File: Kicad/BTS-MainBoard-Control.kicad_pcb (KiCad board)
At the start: 2 copper layers, 26.8 x 45.1 mm, 26 parts, among them J3 Molex Micro Lock (1.25mm 1.5A), J4 Conn_01x14, Q1 DMG3402L, U1 HIP4080A

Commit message: Updated Gerbers and sent files to fab
Signed-off-by: bebenlebricolo <benoittarrade@hotmail.fr>
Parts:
- added REF**: OSHW-Logo2_14.6x12mm_SilkScreen, Symbol:OSHW-Logo2_14.6x12mm_SilkScreen, B.Cu at (75.9, 74.4)

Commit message: Created BOM
Signed-off-by: bebenlebricolo <benoittarrade@hotmail.fr>
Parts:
- removed REF**: OSHW-Logo2_14.6x12mm_SilkScreen, Symbol:OSHW-Logo2_14.6x12mm_SilkScreen
- J3: value Molex Micro Lock (1.25mm 1.5A) -> Input Signals Connector
- J4: value Conn_01x14 -> Out connector
- Q1: value DMG3402L -> DMG3418L-7

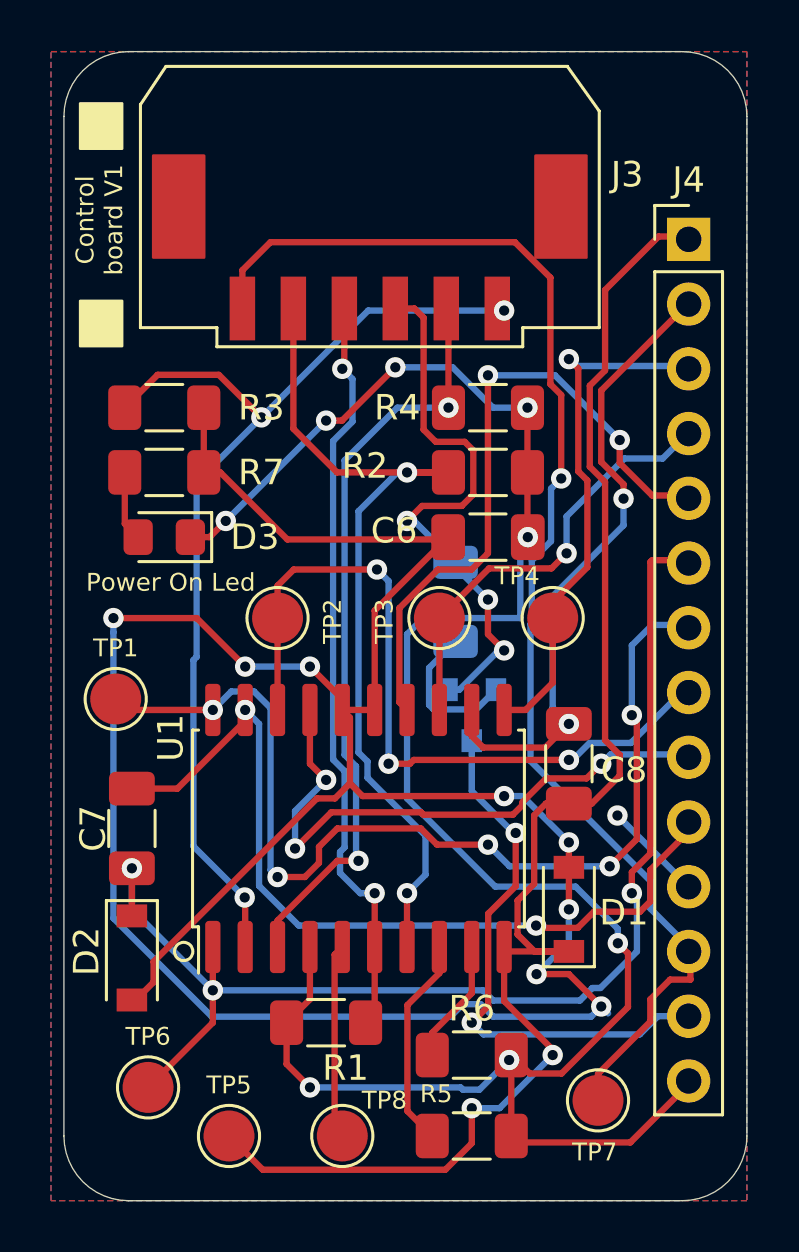
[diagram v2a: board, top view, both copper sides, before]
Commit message: Updated the board to Revsision 1.1 : changed driver ICs
Signed-off-by: bebenlebricolo <benoittarrade@hotmail.fr>
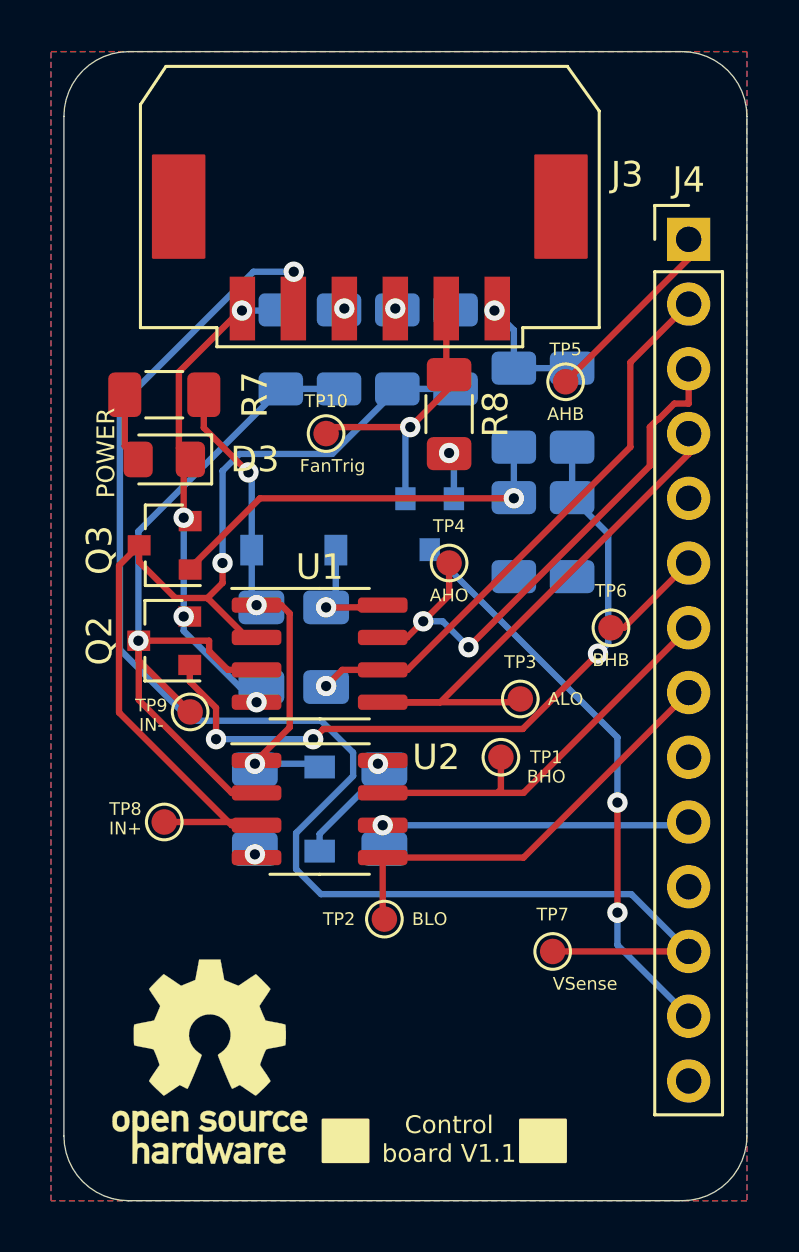
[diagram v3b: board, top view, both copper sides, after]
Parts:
- removed C8: 330nF, Capacitor_SMD:C_1206_3216Metric_Pad1.33x1.80mm_HandSolder
- added C1: 100nF, Capacitor_SMD:C_1206_3216Metric_Pad1.33x1.80mm_HandSolder, B.Cu at (69.6, 66.5)
- added C2: 330nF, Capacitor_SMD:C_1206_3216Metric_Pad1.33x1.80mm_HandSolder, B.Cu at (74.7, 66.5)
- added Q2: BC817, Package_TO_SOT_SMD:SOT-23, F.Cu at (66.0, 59.9)
- added Q3: BC817, Package_TO_SOT_SMD:SOT-23, F.Cu at (66.1, 56.2)
- added R10: 1k, Resistor_SMD:R_1206_3216Metric_Pad1.30x1.75mm_HandSolder, B.Cu at (72.9, 48.5)
- added R9: 1k, Resistor_SMD:R_1206_3216Metric_Pad1.30x1.75mm_HandSolder, B.Cu at (75.2, 48.5)
- added REF**: OSHW-Logo_7.5x8mm_SilkScreen, Symbol:OSHW-Logo_7.5x8mm_SilkScreen, F.Cu at (67.8, 76.5)
- added TP10: TestPoint, TestPoint:TestPoint_Pad_D1.0mm, F.Cu at (72.4, 51.8)
- added TP9: TestPoint, TestPoint:TestPoint_Pad_D1.0mm, F.Cu at (67.1, 62.7)
- added U2: IRS2001, Package_SO:SOIC-8_3.9x4.9mm_P1.27mm, F.Cu at (72.1, 66.5)
- C6, C7, D1, D2, R4: moved to B.Cu
- R1, R2, R6: value 10k -> 56k; moved to B.Cu
- R3, R5: value 10k -> 1k; moved to B.Cu
- R8: moved to F.Cu
- TP1, TP2, TP3, TP4, TP5, TP6, TP7, TP8: footprint TestPoint:TestPoint_Pad_D2.0mm -> TestPoint:TestPoint_Pad_D1.0mm
- U1: value HIP4080A -> IRS2001; footprint Package_SO:SOIC-20W_7.5x12.8mm_P1.27mm -> Package_SO:SOIC-8_3.9x4.9mm_P1.27mm
- moved TP5 32.4 mm to (81.8, 49.8)
- moved R5 28.6 mm to (79.8, 50.8), turned to 90 degrees
- moved R1 26.9 mm to (77.5, 48.5), turned to 90 degrees
- moved TP6 25.6 mm to (83.6, 59.4)
- moved R6 20.4 mm to (79.8, 55.9), turned to 270 degrees
- moved D2 17.2 mm to (71.1, 56.4), turned to 180 degrees
- moved R3 16.0 mm to (82.0, 50.8), turned to 90 degrees
- moved TP1 15.3 mm to (79.2, 64.5)
- moved TP8 14.2 mm to (66.0, 67.1)
- moved TP2 12.5 mm to (74.7, 70.9)
- moved D1 10.5 mm to (72.1, 66.5)
- moved C7 10.4 mm to (72.4, 60.2), turned to 270 degrees
- moved C6 9.88 mm to (69.8, 60.2), turned to 270 degrees
- moved R2 9.45 mm to (70.6, 48.5), turned to 90 degrees
- moved Q1 7.67 mm to (76.5, 55.4)
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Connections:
- C7 pad 1: /BHB -> Net-(C7-Pad1)
- C7 pad 2: /BHS -> /AHS
- D1 pad 1: /AHB -> Net-(C2-Pad1)
- D2 pad 1: /BHB -> Net-(C7-Pad1)
- J3 pad 1: /HEN -> /Inhibit
- J3 pad 2: /Disable -> /Fan_trigger
- J3 pad 3: /Fan_trigger -> /IN+
- J3 pad 4: /IN+ -> /IN-
- J3 pad 5: /IN- -> /VSense
- J3 pad 6: /VSense -> GND
- J4 pad 5: /ALS -> (no net)
- J4 pad 9: /BLS -> (no net)
- R1 pad 1: /IN+ -> /ProtectedIN+
- R2 pad 1: /IN- -> /ProtectedIN-
- R3 pad 1: +12V -> Net-(Q2-Pad1)
- R3 pad 2: /HEN -> /Inhibit
- R4 pad 1: /Disable -> Net-(Q2-Pad1)
- R5 pad 1: Net-(R5-Pad1) -> Net-(Q3-Pad1)
- R5 pad 2: GND -> /Inhibit
- R6 pad 1: Net-(R6-Pad1) -> Net-(Q3-Pad1)
- TP8 pad 1: /OUT -> /ProtectedIN+
- U1 pad 1: /BHB -> +12V
- U1 pad 2: /HEN -> /ProtectedIN+
- U1 pad 3: /Disable -> /ProtectedIN-
- U1 pad 5: /OUT -> /ALO
- U1 pad 6: /IN+ -> /AHS
- U1 pad 7: /IN- -> /AHO
- U1 pad 8: Net-(R5-Pad1) -> Net-(C7-Pad1)
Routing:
- net +12V: track 105.0 -> 19.8 mm, vias 9 -> 3
- net GND: track 88.4 -> 23.0 mm, vias 8 -> 6
- net /AHB: track 58.8 -> 7.59 mm, vias 2 -> 0
- net /BHB: track 49.4 -> 4.10 mm, vias 3 -> 0
- net /HEN: track 40.9 -> 0.00 mm, vias 3 -> 0
- net /ProtectedIN+: track 0.00 -> 40.0 mm, vias 0 -> 1
- net /IN-: track 34.2 -> 0.23 mm, vias 2 -> 1
- net /ProtectedIN-: track 0.00 -> 31.9 mm, vias 0 -> 1
- net /Disable: track 30.0 -> 0.00 mm, vias 2 -> 0
- net /IN+: track 29.8 -> 0.10 mm, vias 2 -> 1
- net Net-(Q2-Pad1): track 0.00 -> 28.6 mm, vias 0 -> 3
- net /ALS: track 25.9 -> 0.00 mm, vias 2 -> 0
- net /BHO: track 40.2 -> 16.1 mm, vias 5 -> 0
- net /BLS: track 23.4 -> 0.00 mm, vias 3 -> 0
- net /BHS: track 33.4 -> 13.0 mm, vias 2 -> 1
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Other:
- board text added: "AHB"
- board text added: "AHO"
- board text added: "ALO"
- board text added: "BHB"
- board text added: "BHO"
- board text added: "BLO"
- board text added: "Beer Thermoregulation System main board (control) V1.1"
- board text added: "Control board V1.1"
- board text added: "FanTrig"
- board text added: "IN+"
- board text added: "IN-"
- board text added: "POWER"
- board text added: "VSense"
- board text removed: "Beer Thermoregulation System main board (control) V1"
- board text removed: "Control board V1"
- board text removed: "Power On Led"
